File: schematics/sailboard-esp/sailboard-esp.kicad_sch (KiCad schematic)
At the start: 16 parts

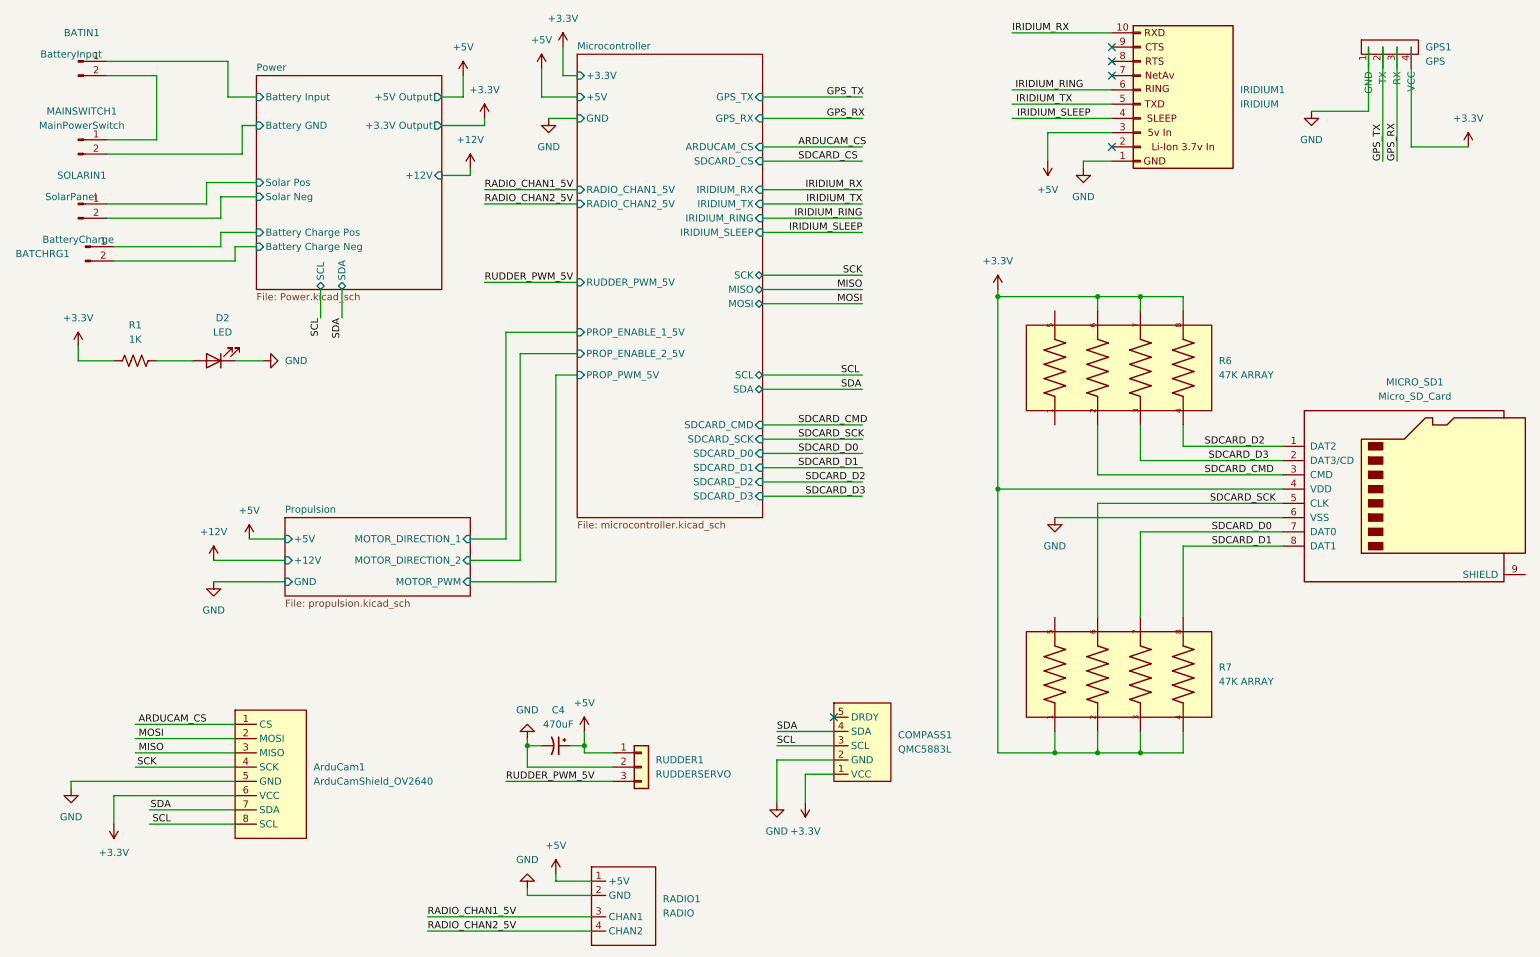
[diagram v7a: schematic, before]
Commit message: rearrange pins to avoid ESP32 reserved / wonky pins.
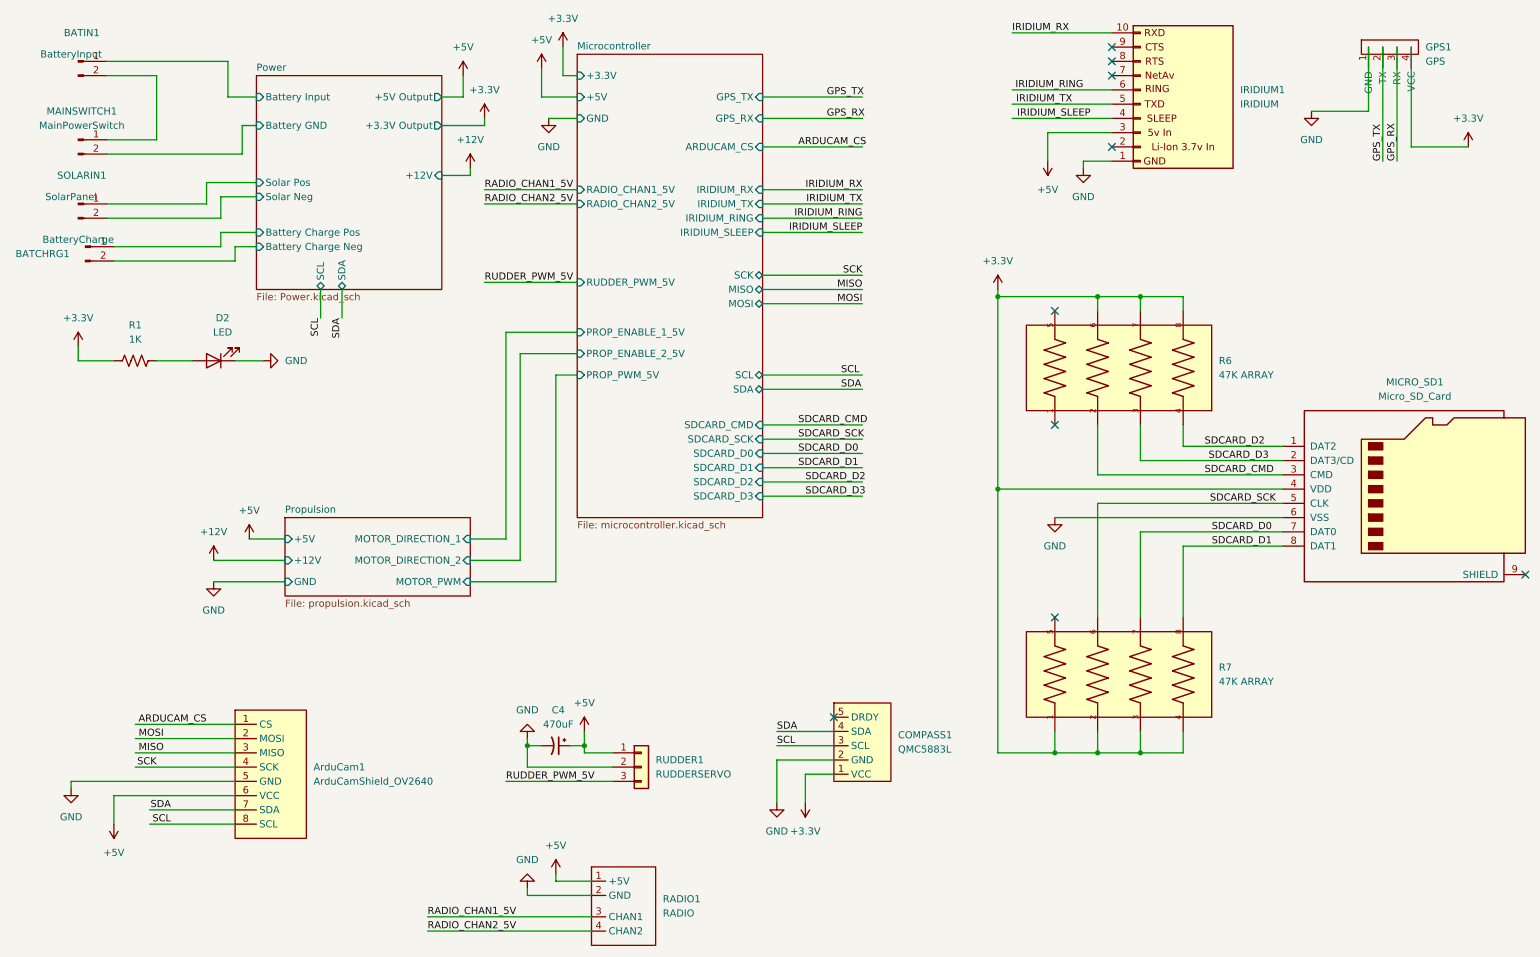
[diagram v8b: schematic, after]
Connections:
- net +3.3V: no longer ArduCam1.6 (VCC)
- net +5V: now also ArduCam1.6 (VCC)
- no-connect marks 5 -> 9
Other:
- sheet Microcontroller ports: added none; removed SDCARD_CS
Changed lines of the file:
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@@
   (no_connect (at 205.74 43.18))
   (no_connect (at 205.74 30.48))
+  (no_connect (at 195.58 127))
+  (no_connect (at 195.58 92.71))
+  (no_connect (at 195.58 72.39))
+  (no_connect (at 279.4 119.38))
   (wire (pts (xy 195.58 109.22) (xy 236.22 109.22))
     (stroke (width 0) (type default) (color 0 0 0 0))
@@
     (stroke (width 0) (type default) (color 0 0 0 0))
   )
-  (wire (pts (xy 143.51 45.72) (xy 161.29 45.72))
-    (stroke (width 0) (type default) (color 0 0 0 0))
-  )
   (wire (pts (xy 21.59 78.74) (xy 21.59 81.28))
     (stroke (width 0) (type default) (color 0 0 0 0))
@@
   )
   (label "ARDUCAM_CS" (at 149.86 43.18 0)
-    (effects (font (size 1.27 1.27)) (justify left bottom))
-  )
-  (label "SDCARD_CS" (at 149.86 45.72 0)
     (effects (font (size 1.27 1.27)) (justify left bottom))
   )
@@
     (pin "1")
   )
+  (symbol (lib_id "power:+5V") (at 27.94 163.83 180) (unit 1)
+    (in_bom yes) (on_board yes) (fields_autoplaced)
+    (property "Reference" "#PWR0119" (id 0) (at 27.94 160.02 0)
+      (effects (font (size 1.27 1.27)) hide)
+    )
+    (property "Value" "+5V" (id 1) (at 27.94 168.91 0))
+    (property "Footprint" "" (id 2) (at 27.94 163.83 0)
+      (effects (font (size 1.27 1.27)) hide)
+    )
+    (property "Datasheet" "" (id 3) (at 27.94 163.83 0)
+      (effects (font (size 1.27 1.27)) hide)
+    )
+    (pin "1")
+  )
   (symbol (lib_id "power:GND") (at 20.32 157.48 0) (unit 1)
     (in_bom yes) (on_board yes) (fields_autoplaced)
@@
     )
     (property "Datasheet" "" (id 3) (at 20.32 157.48 0)
-      (effects (font (size 1.27 1.27)) hide)
-    )
-    (pin "1")
-  )
-  (symbol (lib_id "power:+3.3V") (at 27.94 163.83 180) (unit 1)
-    (in_bom yes) (on_board yes) (fields_autoplaced)
-    (property "Reference" "#PWR0119" (id 0) (at 27.94 160.02 0)
-      (effects (font (size 1.27 1.27)) hide)
-    )
-    (property "Value" "+3.3V" (id 1) (at 27.94 168.91 0))
-    (property "Footprint" "" (id 2) (at 27.94 163.83 0)
-      (effects (font (size 1.27 1.27)) hide)
-    )
-    (property "Datasheet" "" (id 3) (at 27.94 163.83 0)
       (effects (font (size 1.27 1.27)) hide)
     )
@@
       (effects (font (size 1.27 1.27)) (justify right))
     )
-    (pin "SDCARD_CS" input (at 143.51 45.72 0)
-      (effects (font (size 1.27 1.27)) (justify right))
-    )
     (pin "SDCARD_SCK" input (at 143.51 95.25 0)
       (effects (font (size 1.27 1.27)) (justify right))
@@
       (reference "#PWR0118") (unit 1) (value "GND") (footprint "")
     )
-    (path "/31021e88-d4b3-4f00-9396-f09f3c00ea3a"
-      (reference "#PWR0119") (unit 1) (value "+3.3V") (footprint "")
+    (path "/29a45326-3052-41e3-b8a4-6768b73f50c2"
+      (reference "#PWR0119") (unit 1) (value "+5V") (footprint "")
     )
     (path "/535de704-a901-4126-b827-664c51cb0c34"
